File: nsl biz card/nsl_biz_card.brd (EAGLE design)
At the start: 88.9 x 50.8 mm, 3 parts, among them U2 ATMEGA328P-AU

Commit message: NSL biz card!
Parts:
- removed U2: ATMEGA328P-AU, Ava:QFP80P900X900X120-32N
- added BAT1: (no value), SparkFun:BATTCON_12MM
- added C1, C2, C4: 15pF, SparkFun:0603-CAP
- added C10, C11, C12: 4.7uF, SparkFun:0603-CAP
- added C13, C14: (no value), badge.lbrbadge_2013:SPARKFUN_0603-CAP
- added C15, C16, C17, C18: 0.1uF, badge.lbrbadge_2013:SPARKFUN_0603-CAP
- added C19: 1uF, badge.lbrbadge_2013:SPARKFUN_0603-CAP
- added C3: 8.2pF, SparkFun:0603-CAP
- added C5: 33pF, SparkFun:0603-CAP
- added C6: 100nF, SparkFun:0603-CAP
- added C7: 10uF, SparkFun:0603-CAP
- added C8, C9: 1uF, SparkFun:0603-CAP
- added D1: USBUG_PRTR5V0U2X, badge.lbrbadge_2013:USBUG_SOT143B
- added IC1: (no value), badge.lbrbadge_2013:OUTLINE_NONOLITH_TQFP-44
- added J$1: SMA_EDGE, SparkFun:SMA-EDGE
- added JP1: (no value), SparkFun:1X06
- added JP2: (no value), badge.lbrbadge_2013:MICROBUILDER_1X02_OVAL
- added JP3: DASPILKER_USB-RECEPTABLE-HIROSE-ZX62-AB-5PA(11), badge.lbrbadge_2013:DASPILKER_HIROSE-ZX62-AB-5PA(11)
- added L1, L2: 18nH, SparkFun:0603
- added L3: 56nH, SparkFun:0603
- added L4: 220nH, SparkFun:0603
- added LED1, LED2, LED3: (no value), badge.lbrbadge_2013:LED_CHIP-LED0805
- added R1: 100k, SparkFun:0603-RES
- added R2: 820K, SparkFun:0603-RES
- added S1, S2, S3, S4: SWITCH-MOMENTARY-2, SparkFun:TACTILE_SWITCH_TALL
- added SJ1: (no value), badge.lbrbadge_2013:MICROBUILDER_SOLDERJUMPER_REFLOW
- added U$3: CRYSTAL_3.2X2.5-TCXO, picoAVA-R8:CRYSTAL_3.2X2.5-TCXO
- added U$4: SPARKFUN_AP7333-33SOT23-3, badge.lbrbadge_2013:SPARKFUN_SOT23-3
- added X1: M6-RF315_NX3225GA, badge.lbrbadge_2013:M6-RF315_NX3225GA
- moved U$1 2.56 mm to (19.4, 11.4)
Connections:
- removed net AVCC: U2.18
- removed net VCC_2: U2.4
- removed net VDD: U1.9
- removed net VLSS: U1.29
- removed net VSS: U1.8
- new net +: BAT1.PWR@1
- new net +5V: D1.3, JP3.P$1, U$4.1
- new net ANTENNA: SJ1.1
- new net BT1: IC1.41, S4.B2
- new net BT2: IC1.42, S3.B2
- new net BT3: IC1.43, S2.B2
- new net BT4: IC1.44, S1.B2
- new net D+: D1.4, IC1.27, JP3.P$4
- new net D-: D1.2, IC1.26, JP3.P$2
- new net D/C: IC1.7, U1.15
- new net DAT: IC1.34, JP2.1
- new net DGND: X1.2, X1.4
- new net DISP_CS: IC1.4, U1.13
- new net GND: BAT1.GND, C10.2, C11.2, C12.2, C13.1, C14.1, C15.2, C16.2, C17.2, C18.2, C19.2, C2.2, C3.2, C5.2, C6.2, C7.2, D1.1, IC1.18, IC1.30, IC1.38, IC1.8, J$1.GND@0, J$1.GND@1, J$1.GND@2, J$1.GND@3, JP1.1, JP1.2, JP3.P$5, LED1.C, LED2.C, LED3.C, R1.2, R2.1, S1.A2, S2.A2, S3.A2, S4.A2, U$1.18, U$1.21, U$3.1, U$3.2, U$4.3, U1.1, U1.10, U1.11, U1.12, U1.29, U1.30, U1.8
- new net GPIO0: U$1.9
- new net GPIO1: U$1.10
- new net LNK: IC1.29, JP1.6
- new net MISO: IC1.16, U$1.13
- new net MOSI: IC1.15, U$1.14
- new net N$10: IC1.2, LED2.A
- new net N$11: IC1.1, LED1.A
- new net N$12: C12.1, U1.28
- new net N$13: IC1.35, JP2.2
- new net N$14: C9.1, U1.2
- new net N$15: C9.2, U1.3
- new net N$16: C8.1, U1.4
- new net N$17: C8.2, U1.5
- new net N$18: C11.1, U1.27
- new net N$19: R2.2, U1.26
- new net N$2: C1.1, U$3.3
- new net N$20: J$1.SIG, L1.1, SJ1.2
- new net N$3: C4.2, L4.2, U$1.4
- new net N$4: C4.1, L3.2
- new net N$5: C3.1, L2.2, L3.1
- new net N$6: C2.1, L1.2, L2.1
- new net N$7: C13.2, IC1.36, X1.3
- new net N$8: IC1.3, LED3.A
- new net N$9: C14.2, IC1.37, X1.1
- new net RES: IC1.5, U1.14
- new net RF_SEL: IC1.14, U$1.15
- new net RX: IC1.32, JP1.4
- new net SCK: IC1.17, U$1.12
- new net SCL: IC1.11
- new net SCLK/DB0: IC1.21, U1.18
- new net SDA: IC1.10
- new net SDIN/DB1: IC1.23, U1.19
- new net SHUTDOWN: IC1.6, R1.1, U$1.1
- new net TX: IC1.33, JP1.5
- new net XIN: C1.2, U$1.17
- new net XOUT: U$1.16
- net VCC: now also C10.1, C15.1, C16.1, C17.1, C18.1, C19.1, C5.1, C6.1, C7.1, IC1.19, IC1.31, IC1.39, IC1.9, JP1.3, L4.1, U$1.6, U$1.8, U$3.4, U$4.2, U1.6, U1.9; no longer U1.28, U2.6
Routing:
- net N$21: track 0.00 -> 87.3 mm
- net N$1: track 64.8 -> 0.00 mm
- net VCC: track 0.00 -> 46.4 mm, vias 0 -> 2
- net SHUTDOWN: track 0.00 -> 32.6 mm
- net RF_SEL: track 0.00 -> 9.28 mm
- net N$14: track 0.00 -> 6.36 mm
- net N$20: track 0.00 -> 6.16 mm
- net N$19: track 0.00 -> 4.95 mm
- net N$15: track 0.00 -> 4.93 mm
- net N$12: track 0.00 -> 4.85 mm
- net SCK: track 0.00 -> 4.85 mm
- net N$5: track 0.00 -> 4.72 mm
- net N$6: track 0.00 -> 4.72 mm
- net N$3: track 0.00 -> 4.41 mm
- net N$17: track 0.00 -> 4.25 mm
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- added copper zone on layer 1, net GND
- added copper zone on layer 16, net GND
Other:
- board text added: "1"
- board text added: "6"
- board text added: "Meetings Every Tuesday!"

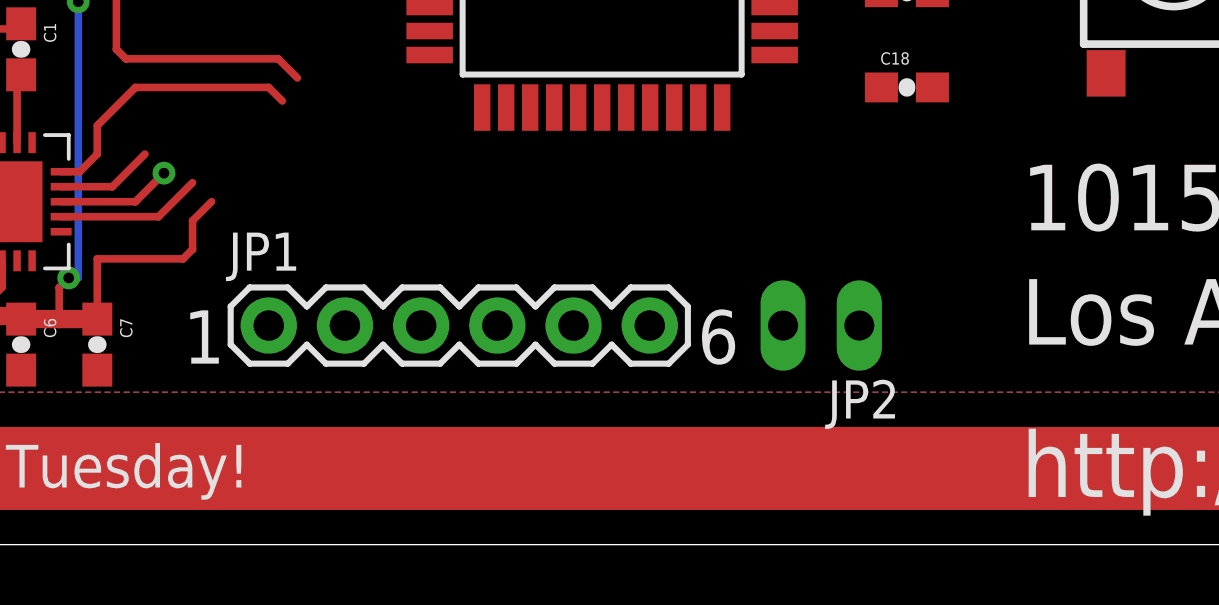
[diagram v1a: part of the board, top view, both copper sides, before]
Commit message: updated programming header
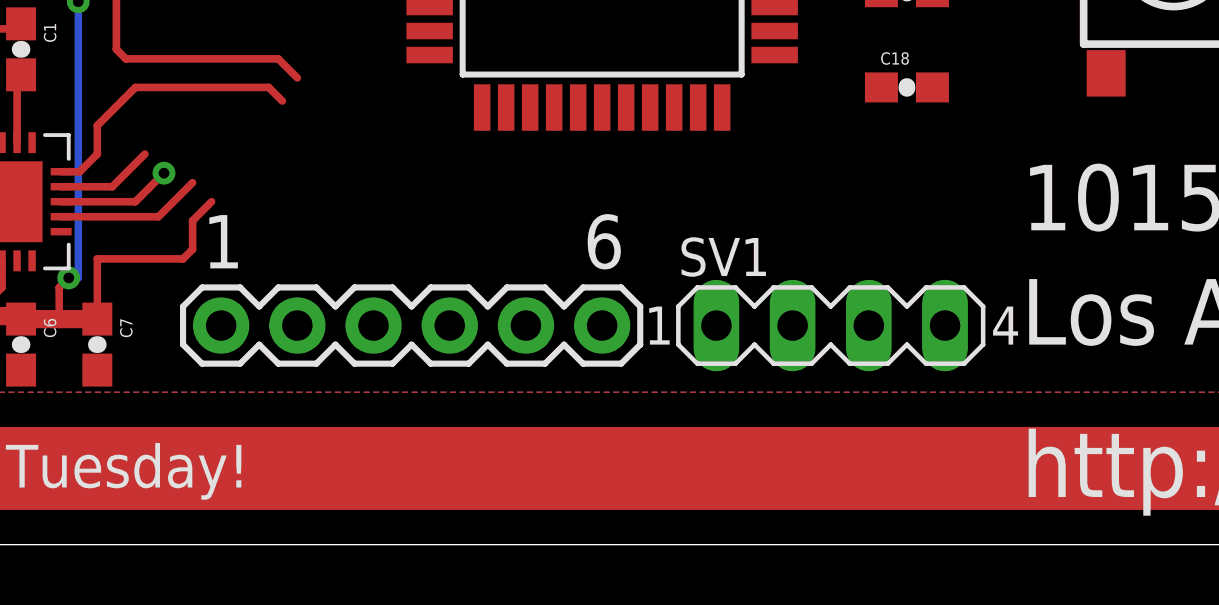
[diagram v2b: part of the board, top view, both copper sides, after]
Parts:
- removed JP2: (no value), badge.lbrbadge_2013:MICROBUILDER_1X02_OVAL
- added SV1: (no value), con-lstb:MA04-1
- moved JP1 1.59 mm to (26.7, 7.30)
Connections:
- net DAT: now also SV1.2; no longer JP2.1
- net GND: now also SV1.1
- net N$13: now also SV1.3; no longer JP2.2
- net VCC: now also SV1.4
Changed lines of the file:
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@@
 <text x="53.34" y="1.5875" size="2.1844" layer="25">http://032.la</text>
 <text x="67.945" y="40.64" size="0.8128" layer="25">528 491</text>
-<text x="25.4" y="6.0325" size="1.778" layer="25">1</text>
-<text x="42.545" y="6.0325" size="1.778" layer="25">6</text>
+<text x="26.035" y="9.2075" size="1.778" layer="25">1</text>
+<text x="38.735" y="9.2075" size="1.778" layer="25">6</text>
 <text x="5.3975" y="1.905" size="1.4224" layer="25">Meetings Every Tuesday!</text>
 </plain>
@@
 <element name="L4" library="SparkFun" package="0603" value="220nH" x="14.9225" y="7.9375" rot="R90"/>
 <element name="R1" library="SparkFun" package="0603-RES" value="100k" x="13.0175" y="16.51" rot="R90"/>
-<element name="JP1" library="SparkFun" package="1X06" value="" x="28.2575" y="7.3025"/>
+<element name="JP1" library="SparkFun" package="1X06" value="" x="26.67" y="7.3025" smashed="yes">
+<attribute name="VALUE" x="25.4" y="4.1275" size="1.27" layer="27"/>
+</element>
 <element name="C8" library="SparkFun" package="0603-CAP" value="1uF" x="77.47" y="28.8925" rot="R180"/>
 <element name="C9" library="SparkFun" package="0603-CAP" value="1uF" x="80.9625" y="28.8925" rot="R180"/>
@@
 <element name="C17" library="badge.lbrbadge_2013" package="SPARKFUN_0603-CAP" value="0.1uF" x="49.53" y="18.415"/>
 <element name="C18" library="badge.lbrbadge_2013" package="SPARKFUN_0603-CAP" value="0.1uF" x="49.53" y="15.24"/>
-<element name="JP2" library="badge.lbrbadge_2013" package="MICROBUILDER_1X02_OVAL" value="" x="46.6725" y="7.3025" rot="R180"/>
 <element name="JP3" library="badge.lbrbadge_2013" package="DASPILKER_HIROSE-ZX62-AB-5PA(11)" value="DASPILKER_USB-RECEPTABLE-HIROSE-ZX62-AB-5PA(11)" x="7.3025" y="50.8" rot="R180"/>
 <element name="U$4" library="badge.lbrbadge_2013" package="SPARKFUN_SOT23-3" value="SPARKFUN_AP7333-33SOT23-3" x="11.1125" y="43.4975"/>
@@
 <element name="J$1" library="SparkFun" package="SMA-EDGE" value="SMA_EDGE" x="1.905" y="7.9375" rot="R90"/>
 <element name="SJ1" library="badge.lbrbadge_2013" package="MICROBUILDER_SOLDERJUMPER_REFLOW" value="" x="5.3975" y="9.2075" rot="R90"/>
+<element name="SV1" library="con-lstb" package="MA04-1" value="" x="46.99" y="7.3025">
+<attribute name="OC_NEWARK" value="unknown" x="46.99" y="7.3025" size="1.778" layer="27" display="off"/>
+<attribute name="MPN" value="" x="46.99" y="7.3025" size="1.778" layer="27" display="off"/>
+<attribute name="MF" value="" x="46.99" y="7.3025" size="1.778" layer="27" display="off"/>
+<attribute name="OC_FARNELL" value="unknown" x="46.99" y="7.3025" size="1.778" layer="27" display="off"/>
+</element>
 </elements>
 <signals>
@@
 <contactref element="C18" pad="1"/>
 <contactref element="JP1" pad="3"/>
+<contactref element="SV1" pad="4"/>
 <wire x1="48.68" y1="23.495" x2="74.8275" y2="28.8925" width="0" layer="19" extent="1-1"/>
 <wire x1="48.68" y1="20.955" x2="48.68" y2="23.495" width="0" layer="19" extent="1-1"/>
@@
 <wire x1="26.7725" y1="19.05" x2="33.62" y2="17.92" width="0" layer="19" extent="1-1"/>
 <wire x1="21.9075" y1="18.0975" x2="26.7725" y2="19.05" width="0" layer="19" extent="1-1"/>
-<wire x1="33.3375" y1="7.3025" x2="25.7175" y2="9.8425" width="0" layer="19" extent="1-1"/>
+<wire x1="31.75" y1="7.3025" x2="25.7175" y2="9.8425" width="0" layer="19" extent="1-1"/>
+<wire x1="50.8" y1="7.3025" x2="14.9225" y2="7.0875" width="0" layer="19" extent="1-1"/>
 <wire x1="12.0625" y1="42.4975" x2="15.5575" y2="18.7325" width="0" layer="19" extent="1-1"/>
 </signal>
@@
 <contactref element="J$1" pad="GND@2"/>
 <contactref element="J$1" pad="GND@1"/>
+<contactref element="SV1" pad="1"/>
 <wire x1="75.1" y1="32.82" x2="80" y2="32.82" width="0" layer="19" extent="1-1"/>
 <wire x1="73.7" y1="32.82" x2="75.1" y2="32.82" width="0" layer="19" extent="1-1"/>
@@
 <wire x1="22.5425" y1="5.8175" x2="20.0025" y2="5.8175" width="0" layer="19" extent="1-1"/>
 <wire x1="17.4625" y1="5.8175" x2="20.0025" y2="5.8175" width="0" layer="19" extent="1-1"/>
-<wire x1="28.2575" y1="7.3025" x2="22.5425" y2="5.8175" width="0" layer="19" extent="1-1"/>
-<wire x1="30.7975" y1="7.3025" x2="28.2575" y2="7.3025" width="0" layer="19" extent="1-1"/>
+<wire x1="26.67" y1="7.3025" x2="22.5425" y2="5.8175" width="0" layer="19" extent="1-1"/>
+<wire x1="29.21" y1="7.3025" x2="26.67" y2="7.3025" width="0" layer="19" extent="1-1"/>
 <wire x1="7.7225" y1="8.5725" x2="9.4225" y2="14.2875" width="0" layer="19" extent="1-1"/>
-<wire x1="7.3025" y1="29.21" x2="20.32" y2="27.085" width="0" layer="19" extent="1-16"/>
+<wire x1="1.905" y1="7.9375" x2="7.7225" y2="8.5725" width="0" layer="19" extent="1-1"/>
+<wire x1="1.905" y1="7.9375" x2="1.905" y2="7.9375" width="0" layer="19" extent="1-16"/>
+<wire x1="1.905" y1="13.0175" x2="1.905" y2="7.9375" width="0" layer="19" extent="1-16"/>
+<wire x1="1.905" y1="13.0175" x2="1.905" y2="13.0175" width="0" layer="19" extent="1-16"/>
+<wire x1="43.18" y1="7.3025" x2="1.905" y2="7.9375" width="0" layer="19" extent="1-1"/>
+<wire x1="7.3025" y1="29.21" x2="13.0175" y2="18.7325" width="0" layer="19" extent="16-16"/>
 <wire x1="8.0525" y1="44.4975" x2="7.3025" y2="29.21" width="0" layer="19" extent="1-16"/>
 <wire x1="8.6025" y1="46.675" x2="8.0525" y2="44.4975" width="0" layer="19" extent="1-16"/>
 <wire x1="11.1125" y1="44.5975" x2="8.0525" y2="44.4975" width="0" layer="19" extent="1-1"/>
-<wire x1="1.905" y1="13.0175" x2="7.7225" y2="8.5725" width="0" layer="19" extent="1-16"/>
-<wire x1="1.905" y1="13.0175" x2="1.905" y2="13.0175" width="0" layer="19" extent="1-16"/>
-<wire x1="1.905" y1="7.9375" x2="1.905" y2="13.0175" width="0" layer="19" extent="1-16"/>
-<wire x1="1.905" y1="7.9375" x2="1.905" y2="7.9375" width="0" layer="19" extent="1-16"/>
 </signal>
 <signal name="SCK">
@@
 <signal name="N$13">
 <contactref element="IC1" pad="35"/>
-<contactref element="JP2" pad="2"/>
-<wire x1="45.4025" y1="7.3025" x2="42.57" y2="26.07" width="0" layer="19" extent="1-1"/>
+<contactref element="SV1" pad="3"/>
+<wire x1="48.26" y1="7.3025" x2="42.57" y2="26.07" width="0" layer="19" extent="1-1"/>
 </signal>
 <signal name="DAT">
 <contactref element="IC1" pad="34"/>
-<contactref element="JP2" pad="1"/>
-<wire x1="47.9425" y1="7.3025" x2="43.37" y2="26.07" width="0" layer="19" extent="1-1"/>
+<contactref element="SV1" pad="2"/>
+<wire x1="45.72" y1="7.3025" x2="43.37" y2="26.07" width="0" layer="19" extent="1-1"/>
 </signal>
 <signal name="+5V">
@@
 <contactref element="IC1" pad="32"/>
 <contactref element="JP1" pad="4"/>
-<wire x1="35.8775" y1="7.3025" x2="45.12" y2="23.52" width="0" layer="19" extent="1-1"/>
+<wire x1="34.29" y1="7.3025" x2="45.12" y2="23.52" width="0" layer="19" extent="1-1"/>
 </signal>
 <signal name="TX">
 <contactref element="IC1" pad="33"/>
 <contactref element="JP1" pad="5"/>
-<wire x1="38.4175" y1="7.3025" x2="45.12" y2="24.32" width="0" layer="19" extent="1-1"/>
+<wire x1="36.83" y1="7.3025" x2="45.12" y2="24.32" width="0" layer="19" extent="1-1"/>
 </signal>
 <signal name="LNK">
 <contactref element="IC1" pad="29"/>
 <contactref element="JP1" pad="6"/>
-<wire x1="40.9575" y1="7.3025" x2="45.12" y2="21.12" width="0" layer="19" extent="1-1"/>
+<wire x1="39.37" y1="7.3025" x2="45.12" y2="21.12" width="0" layer="19" extent="1-1"/>
 </signal>
 <signal name="BT1">
